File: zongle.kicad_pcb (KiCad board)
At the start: 6 copper layers, 13.5 x 14.4 mm, 20 parts, among them U1 453-00059R

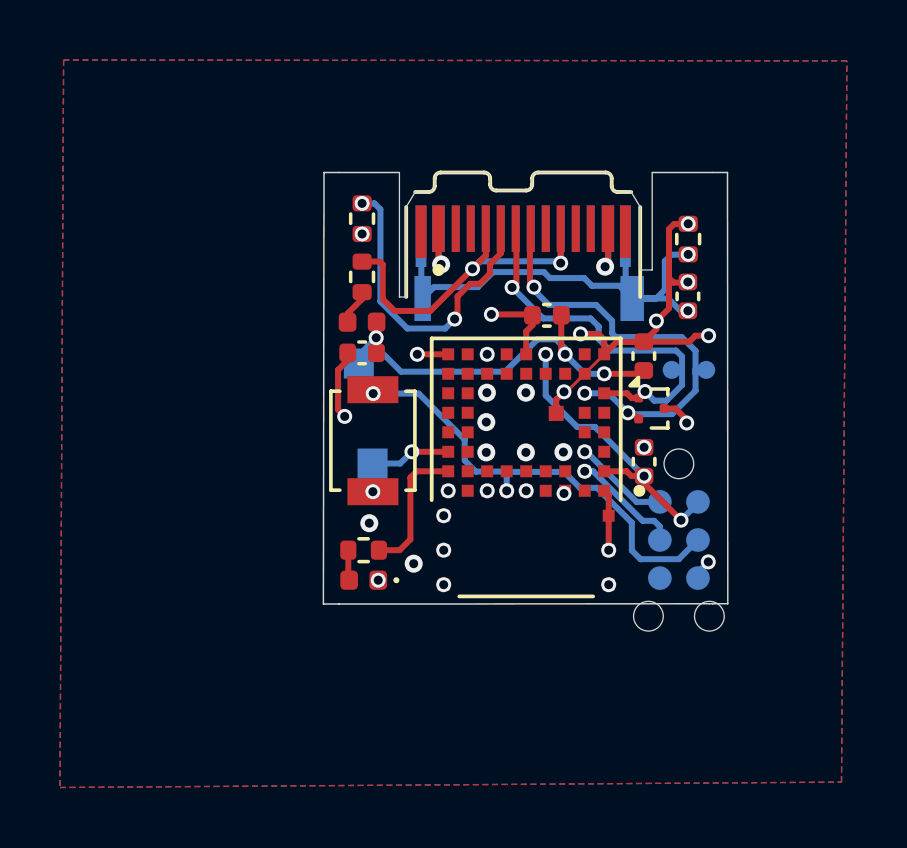
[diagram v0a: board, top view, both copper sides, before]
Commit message: moved all power traces to inner layers. added some via stitching
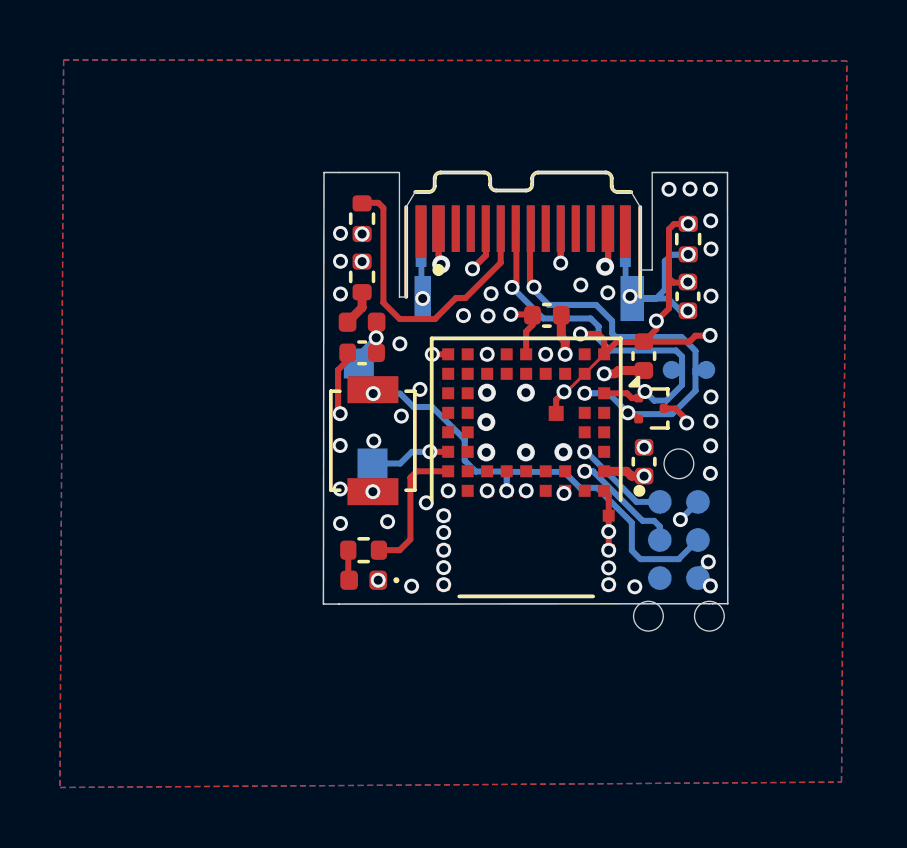
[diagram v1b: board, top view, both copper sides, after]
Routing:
- net GND: track 33.0 -> 57.9 mm, vias 36 -> 68
- net Net-(C26-Pad1): track 16.9 -> 19.5 mm, vias 2 -> 4
- net Net-(USB_C2-CC): track 10.6 -> 10.00 mm, vias 2 -> 0
- net VBUS_Raw: track 13.7 -> 14.1 mm, vias 2 -> 3
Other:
- board text added: "zongle@0.0.3"
- board text removed: "zongle@0.0.2"

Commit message: some more cleanup. changed zone fill properties to match design requirements. moved led trace to power layer, more via stitching
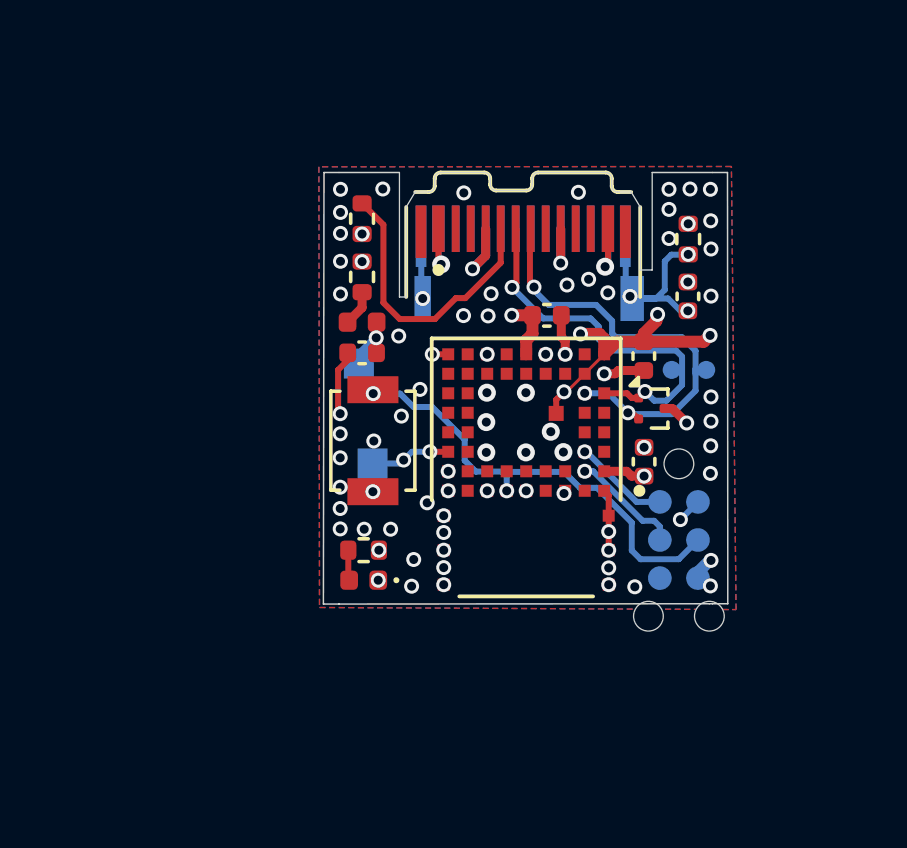
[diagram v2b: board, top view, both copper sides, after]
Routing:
- net GND: track 57.9 -> 28.3 mm, vias 68 -> 82
- net LED_ST: track 4.61 -> 4.51 mm, vias 0 -> 2
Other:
- board text added: "zongle@0.0.4"
- board text removed: "zongle@0.0.3"

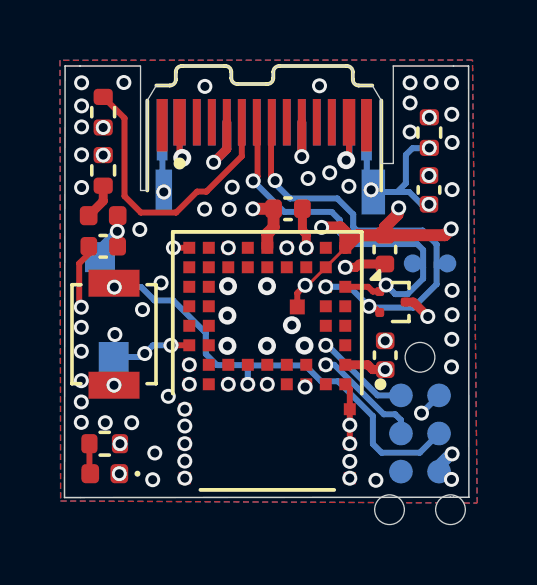
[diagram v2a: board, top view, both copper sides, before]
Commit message: moved led outside of antenna perimeter just to be extra sure. some via stitching + cleanup
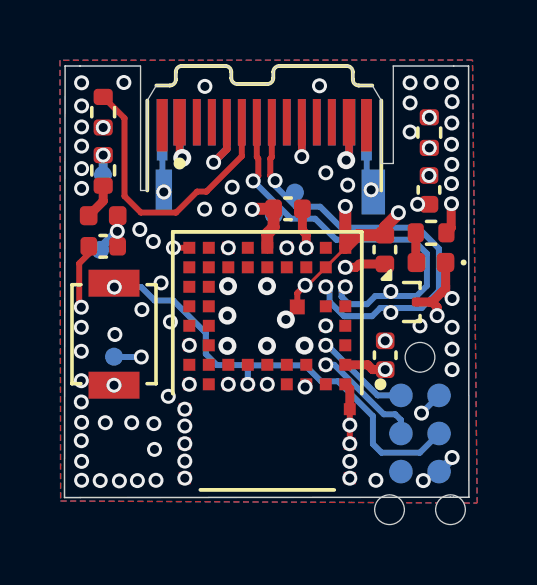
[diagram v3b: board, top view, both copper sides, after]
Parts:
- removed Tp+5v, TpD+, TpD-, TpGND: TestPoint, TestPoint:TestPoint_Pad_1.0x1.0mm
- added Tp+5v1: +5v, TestPoint:TestPoint_Pad_1.0x1.0mm, B.Cu at (146.2, 108.7)
- added TpD+1: D+, TestPoint:TestPoint_Pad_1.0x1.0mm, B.Cu at (152.0, 107.5)
- added TpD-1: D-, TestPoint:TestPoint_Pad_1.0x1.0mm, B.Cu at (152.7, 106.7)
- added TpGND1: Gnd, TestPoint:TestPoint_Pad_1.0x1.0mm, B.Cu at (146.7, 112.2)
- added TpVBUS1: VBUS, TestPoint:TestPoint_Pad_1.0x1.0mm, B.Cu at (146.3, 106.2)
- moved R21 13.0 mm to (157.2, 108.1)
- moved LED_STATUS1 13.0 mm to (157.2, 109.1)
- moved ESD1 0.37 mm to (156.3, 110.4)
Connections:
- U1 pad 10: LED_ST -> unconnected-(U1-SIO_03/AIN1-Pad10)
- U1 pad 51: unconnected-(U1-SIO_32-Pad51) -> LED_ST
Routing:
- net GND: track 28.3 -> 23.3 mm, vias 82 -> 92
- net LED_ST: track 4.51 -> 8.52 mm
- net Net-(C26-Pad1): track 19.5 -> 18.0 mm
- net D+: track 12.9 -> 13.9 mm, vias 2 -> 3
- net +5V: track 14.5 -> 13.8 mm

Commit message: moved testpad for 5v to allow via in pad for decoupeling cap instead of trace to a far away via
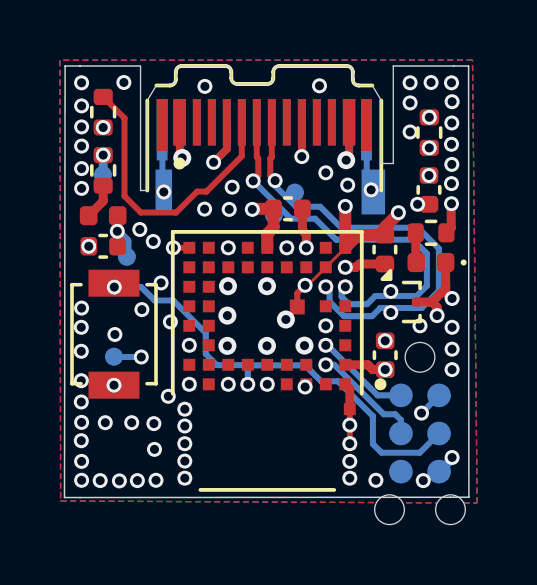
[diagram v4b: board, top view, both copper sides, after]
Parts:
- moved Tp+5v1 0.92 mm to (147.1, 108.9)
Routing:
- net GND: track 23.3 -> 21.1 mm, vias 92 -> 93
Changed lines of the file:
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@@
 	(footprint "TestPoint:TestPoint_Pad_1.0x1.0mm"
 		(layer "B.Cu")
-		(at 146.2 108.65)
+		(at 147.09 108.88)
 		(descr "SMD rectangular pad as test Point, square 1.0mm side length")
 		(tags "test point SMD pad rectangle square")
@@
 		)
 		(property "Value" "+5v"
-			(at 0.1 -0.89 180)
+			(at 0.04 -0.91 180)
 			(layer "B.SilkS")
 			(effects
@@
 	)
 	(segment
-		(start 145.57 110.56)
-		(end 145.57 110.5)
-		(width 0.2)
-		(layer "F.Cu")
-		(net 1)
-	)
-	(segment
 		(start 157.715 109.85)
 		(end 157.715 109.08)
@@
 	)
 	(segment
-		(start 145.5 110.43)
-		(end 145.5 109.1)
-		(width 0.2)
-		(layer "F.Cu")
-		(net 1)
-	)
-	(segment
 		(start 154.37 108.58)
 		(end 154.79 108.16)
@@
 	)
 	(segment
-		(start 145.57 110.5)
-		(end 145.5 110.43)
-		(width 0.2)
-		(layer "F.Cu")
-		(net 1)
-	)
-	(segment
 		(start 154.79 108.16)
 		(end 155.69 108.16)
@@
 	)
 	(segment
-		(start 145.5 109.1)
-		(end 145.82 108.78)
-		(width 0.2)
-		(layer "F.Cu")
-		(net 1)
-	)
-	(segment
 		(start 153.12 109.83)
 		(end 153.03 109.83)
@@
 	)
 	(segment
-		(start 145.82 108.78)
-		(end 145.82 108.53)
-		(width 0.2)
-		(layer "F.Cu")
-		(net 1)
-	)
-	(segment
 		(start 157.92 110.27)
 		(end 157.715 110.065)
@@
 	)
 	(via
+		(at 145.58 110.59)
+		(size 0.5)
+		(drill 0.3)
+		(layers "F.Cu" "B.Cu")
+		(free yes)
+		(net 1)
+	)
+	(via
 		(at 145.57 113.01)
 		(size 0.5)
@@
 	)
 	(via
+		(at 145.82 108.53)
+		(size 0.5)
+		(drill 0.3)
+		(layers "F.Cu" "B.Cu")
+		(net 1)
+	)
+	(via
 		(at 149.02 114.52)
 		(size 0.5)
@@
 		(layers "F.Cu" "B.Cu")
 		(free yes)
-		(net 1)
-	)
-	(via
-		(at 145.57 110.56)
-		(size 0.5)
-		(drill 0.3)
-		(layers "F.Cu" "B.Cu")
 		(net 1)
 	)
@@
 	)
 	(segment
-		(start 146.77 108.03)
-		(end 146.192164 108.607836)
-		(width 0.3)
-		(layer "B.Cu")
+		(start 147.09 108.88)
+		(end 147.09 108.35)
+		(width 0.3)
+		(layer "B.Cu")
+		(net 6)
+	)
+	(segment
+		(start 147.09 108.35)
+		(end 146.77 108.03)
+		(width 0.3)
+		(layer "B.Cu")

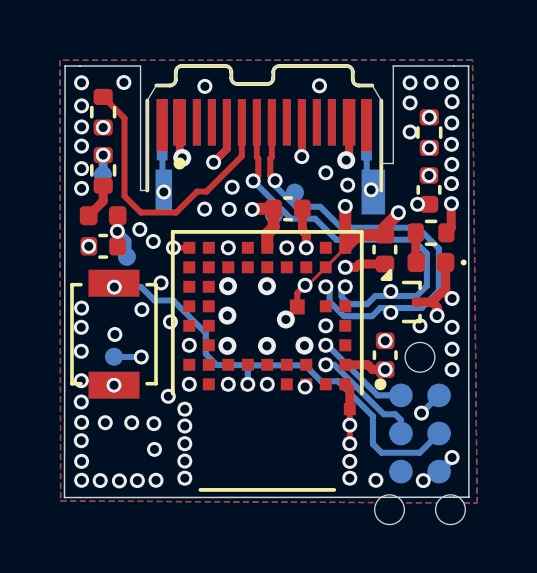
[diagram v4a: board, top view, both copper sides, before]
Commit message: removed usb testpoints
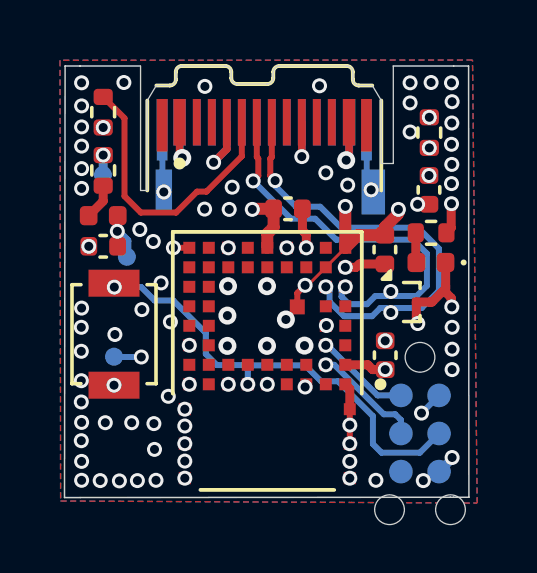
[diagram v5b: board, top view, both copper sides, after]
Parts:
- removed TpD+1: D+, TestPoint:TestPoint_Pad_1.0x1.0mm
- removed TpD-1: D-, TestPoint:TestPoint_Pad_1.0x1.0mm
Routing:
- net GND: track 21.1 -> 21.7 mm, vias 93 -> 92

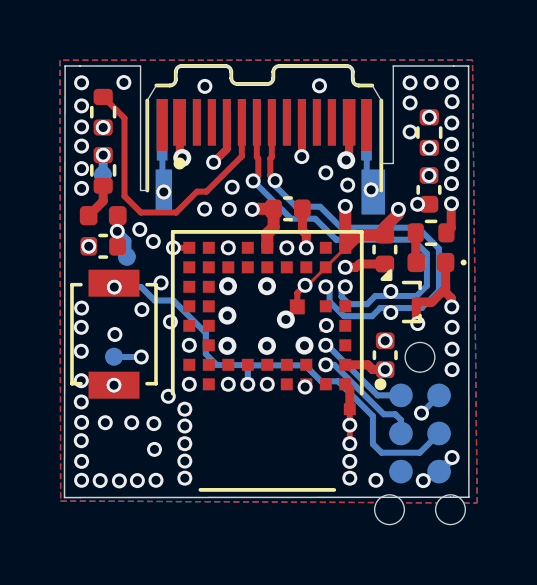
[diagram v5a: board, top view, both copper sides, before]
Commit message: cleaned usb traces. moved esd closer to usb
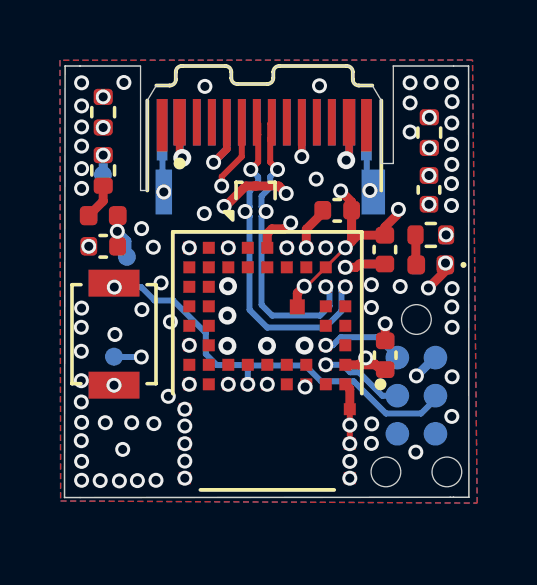
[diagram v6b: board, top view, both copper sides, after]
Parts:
- moved ESD1 6.02 mm to (151.4, 106.9), turned to 0 degrees
- moved C23 1.64 mm to (154.1, 107.3), turned to 0 degrees
- moved SWD1 1.27 mm to (156.7, 113.5)
- moved LED_STATUS1 0.08 mm to (157.2, 109.2)
- moved R21 0.07 mm to (157.2, 108.2)
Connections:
- U1 pad 23: unconnected-(U1-SIO_25-Pad23) -> LED_ST
- U1 pad 51: LED_ST -> unconnected-(U1-SIO_32-Pad51)
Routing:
- net D-: track 15.2 -> 9.94 mm
- net LED_ST: track 8.50 -> 4.63 mm
- net D+: track 13.9 -> 11.3 mm
- net VBUS_Raw: track 14.9 -> 16.2 mm
- net RST: track 14.9 -> 13.8 mm
- net GND: track 21.7 -> 20.8 mm, vias 92 -> 96
- net SWCLK: track 3.72 -> 2.81 mm
- net Net-(USB_C2-CC): track 9.65 -> 10.1 mm, vias 0 -> 2

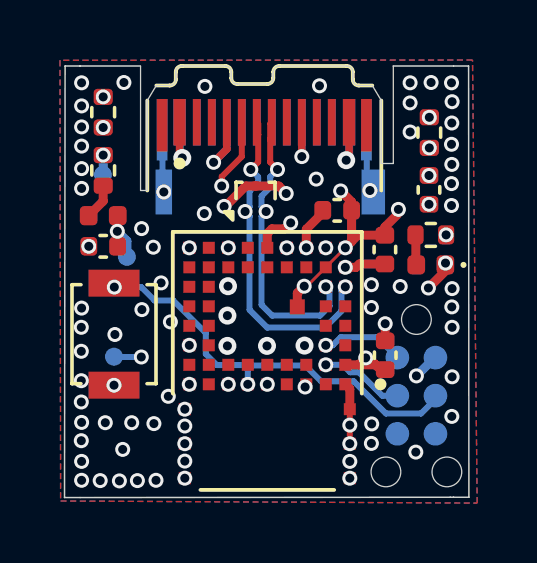
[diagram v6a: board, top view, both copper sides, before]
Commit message: moved testpoints
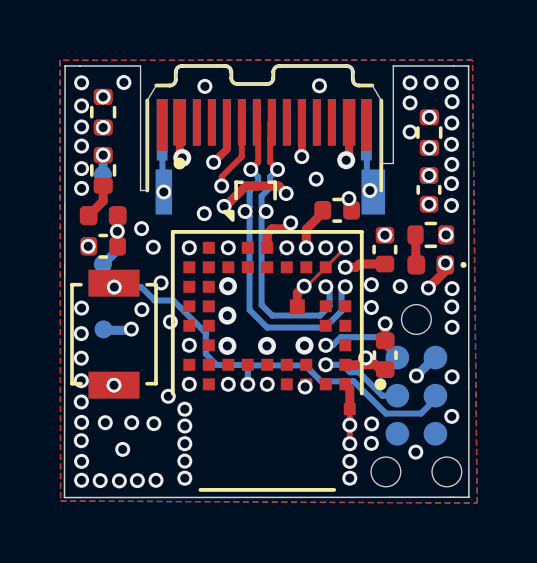
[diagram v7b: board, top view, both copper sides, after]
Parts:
- moved TpGND1 0.97 mm to (146.3, 111.3)
- moved Tp+5v1 0.84 mm to (146.3, 109.1)
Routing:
- net GND: track 20.8 -> 16.7 mm, vias 96 -> 95
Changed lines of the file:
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@@
 	(footprint "TestPoint:TestPoint_Pad_1.0x1.0mm"
 		(layer "B.Cu")
-		(at 146.66 112.21)
+		(at 146.31 111.3)
 		(descr "SMD rectangular pad as test Point, square 1.0mm side length")
 		(tags "test point SMD pad rectangle square")
@@
 	(footprint "TestPoint:TestPoint_Pad_1.0x1.0mm"
 		(layer "B.Cu")
-		(at 147.09 108.88)
+		(at 146.29 109.13)
 		(descr "SMD rectangular pad as test Point, square 1.0mm side length")
 		(tags "test point SMD pad rectangle square")
@@
 	)
 	(segment
+		(start 154.49 106.96)
+		(end 154.58 107.05)
+		(width 0.3)
+		(layer "F.Cu")
+		(net 1)
+	)
+	(segment
 		(start 154.495 104.395)
 		(end 154.495 105.675)
@@
 	)
 	(segment
+		(start 154.58 107.05)
+		(end 154.58 107.33)
+		(width 0.3)
+		(layer "F.Cu")
+		(net 1)
+	)
+	(segment
 		(start 154.4 105.79)
 		(end 154.37 105.82)
@@
 	)
 	(segment
-		(start 154.215 106.685)
-		(end 154.58 107.05)
-		(width 0.3)
-		(layer "F.Cu")
-		(net 1)
-	)
-	(segment
 		(start 154.48 105.66)
 		(end 154.495 105.675)
@@
 	)
 	(segment
-		(start 154.58 108.37)
-		(end 154.37 108.58)
-		(width 0.3)
-		(layer "F.Cu")
-		(net 1)
-	)
-	(segment
-		(start 154.58 107.33)
-		(end 154.58 108.37)
-		(width 0.3)
-		(layer "F.Cu")
-		(net 1)
-	)
-	(segment
 		(start 157.14 109.92)
 		(end 157.705 109.355)
@@
 		(start 150.37 107.2)
 		(end 150.33 107.2)
-		(width 0.3)
-		(layer "F.Cu")
-		(net 1)
-	)
-	(segment
-		(start 154.37 108.58)
-		(end 154.79 108.16)
-		(width 0.3)
-		(layer "F.Cu")
-		(net 1)
-	)
-	(segment
-		(start 154.79 108.16)
-		(end 155.69 108.16)
 		(width 0.3)
 		(layer "F.Cu")
@@
 	)
 	(segment
-		(start 154.58 107.05)
-		(end 154.58 107.33)
-		(width 0.3)
-		(layer "F.Cu")
-		(net 1)
-	)
-	(segment
 		(start 151.92 107.95)
 		(end 151.77 108.1)
@@
 	)
 	(segment
-		(start 156.14 107.3)
-		(end 156.15 107.31)
-		(width 0.4)
-		(layer "F.Cu")
-		(net 1)
-	)
-	(segment
 		(start 153.12 109.83)
 		(end 153.03 109.83)
@@
 	)
 	(segment
+		(start 154.49 106.94)
+		(end 154.49 106.96)
+		(width 0.3)
+		(layer "F.Cu")
+		(net 1)
+	)
+	(segment
 		(start 153 109.86)
 		(end 152.77 110.09)
@@
 	)
 	(segment
-		(start 156.11 107.47)
-		(end 155.69 107.89)
-		(width 0.3)
-		(layer "F.Cu")
-		(net 1)
-	)
-	(segment
 		(start 154.52 115.11)
 		(end 154.52 114.49)
@@
 		(net 1)
 	)
-	(segment
-		(start 155.69 107.89)
-		(end 155.69 108.16)
-		(width 0.3)
-		(layer "F.Cu")
-		(net 1)
-	)
 	(via
 		(at 150.44 110.84)
@@
 	)
 	(via
-		(at 145.57 112.03)
+		(at 145.57 112.26)
 		(size 0.5)
 		(drill 0.3)
@@
 	)
 	(via
+		(at 155.69 108.16)
+		(size 0.5)
+		(drill 0.3)
+		(layers "F.Cu" "B.Cu")
+		(net 1)
+	)
+	(via
 		(at 157.17 104.23)
 		(size 0.5)
@@
 	)
 	(via
-		(at 146.69 111.47)
+		(at 147.24 111.29)
 		(size 0.5)
 		(drill 0.3)
@@
 	)
 	(via
-		(at 145.82 108.53)
+		(at 145.8 108.53)
 		(size 0.5)
 		(drill 0.3)
@@
 	)
 	(via
-		(at 154.215 106.685)
+		(at 154.49 106.94)
 		(size 0.5)
 		(drill 0.3)
@@
 	)
 	(via
-		(at 145.57 111.23)
+		(at 145.57 111.44)
 		(size 0.5)
 		(drill 0.3)
@@
 		(layers "F.Cu" "B.Cu")
 		(free yes)
-		(net 1)
-	)
-	(via
-		(at 156.14 107.3)
-		(size 0.5)
-		(drill 0.3)
-		(layers "F.Cu" "B.Cu")
 		(net 1)
 	)
@@
 	)
 	(via
-		(at 147.57 112.22)
-		(size 0.5)
-		(drill 0.3)
-		(layers "F.Cu" "B.Cu")
-		(net 1)
-	)
-	(via
 		(at 149.02 115.11)
 		(size 0.5)
@@
 		(end 148.855 105.505)
 		(width 0.2)
+		(layer "B.Cu")
+		(net 1)
+	)
+	(segment
+		(start 147.2 111.33)
+		(end 146.34 111.33)
+		(width 0.3)
 		(layer "B.Cu")
 		(net 1)
@@
 	)
 	(segment
-		(start 147.57 112.22)
-		(end 146.65 112.22)
-		(width 0.2)
+		(start 146.34 111.33)
+		(end 146.31 111.3)
+		(width 0.3)
 		(layer "B.Cu")
 		(net 1)
@@
 	)
 	(segment
+		(start 147.24 111.29)
+		(end 147.2 111.33)
+		(width 0.3)
+		(layer "B.Cu")
+		(net 1)
+	)
+	(segment
 		(start 156.49 103.12)
 		(end 156.53 103.08)
@@
 	)
 	(segment
+		(start 155.19 107.5)
+		(end 156.03 107.5)
+		(width 0.3)
+		(layer "In2.Cu")
+		(net 5)
+	)
+	(segment
+		(start 154.05 107.88)
+		(end 154.81 107.88)
+		(width 0.3)
+		(layer "In2.Cu")
+		(net 5)
+	)
+	(segment
+		(start 153.72 108.58)
+		(end 153.72 108.21)
+		(width 0.3)
+		(layer "In2.Cu")
+		(net 5)
+	)
+	(segment
+		(start 156.03 107.5)
+		(end 156.68 108.15)
+		(width 0.3)
+		(layer "In2.Cu")
+		(net 5)
+	)
+	(segment
+		(start 154.81 107.88)
+		(end 155.19 107.5)
+		(width 0.3)
+		(layer "In2.Cu")
+		(net 5)
+	)
+	(segment
+		(start 156.68 108.15)
+		(end 157.73 108.15)
+		(width 0.3)
+		(layer "In2.Cu")
+		(net 5)
+	)
+	(segment
 		(start 153.72 108.21)
 		(end 154.05 107.88)
@@
 	)
 	(segment
-		(start 155.08 108.15)
-		(end 157.73 108.15)
-		(width 0.3)
-		(layer "In2.Cu")
-		(net 5)
-	)
-	(segment
-		(start 153.72 108.58)
-		(end 153.72 108.21)
-		(width 0.3)
-		(layer "In2.Cu")
-		(net 5)
-	)
-	(segment
-		(start 154.81 107.88)
-		(end 155.08 108.15)
-		(width 0.3)
-		(layer "In2.Cu")
-		(net 5)
-	)
-	(segment
-		(start 154.05 107.88)
-		(end 154.81 107.88)
-		(width 0.3)
-		(layer "In2.Cu")
-		(net 5)
-	)
-	(segment
 		(start 154.37 109.23)
 		(end 154.73 109.23)
@@
 	)
 	(segment
-		(start 147.09 108.88)
-		(end 147.09 108.35)
+		(start 146.77 108.03)
+		(end 146.72 107.98)
 		(width 0.3)
 		(layer "B.Cu")
@@
 	)
 	(segment
-		(start 147.09 108.35)
+		(start 146.77 108.65)
 		(end 146.77 108.03)
 		(width 0.3)
 		(layer "B.Cu")
+		(net 6)
+	)
+	(segment
+		(start 146.29 109.13)
+		(end 146.77 108.65)
+		(width 0.3)
+		(layer "B.Cu")
